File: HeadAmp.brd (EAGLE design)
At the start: 37.8 x 25.7 mm, 31 parts, among them U1 MAX97220A

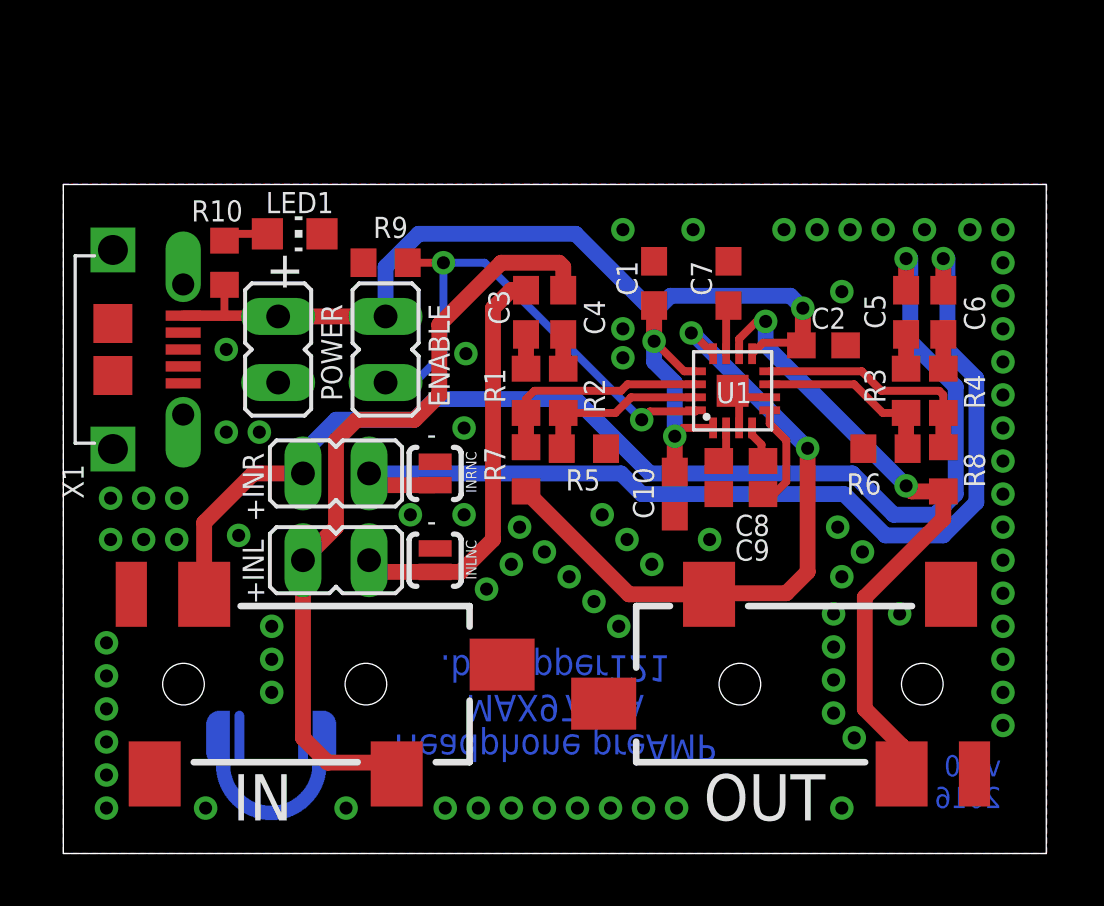
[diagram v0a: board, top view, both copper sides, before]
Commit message: Changed Gain to Max
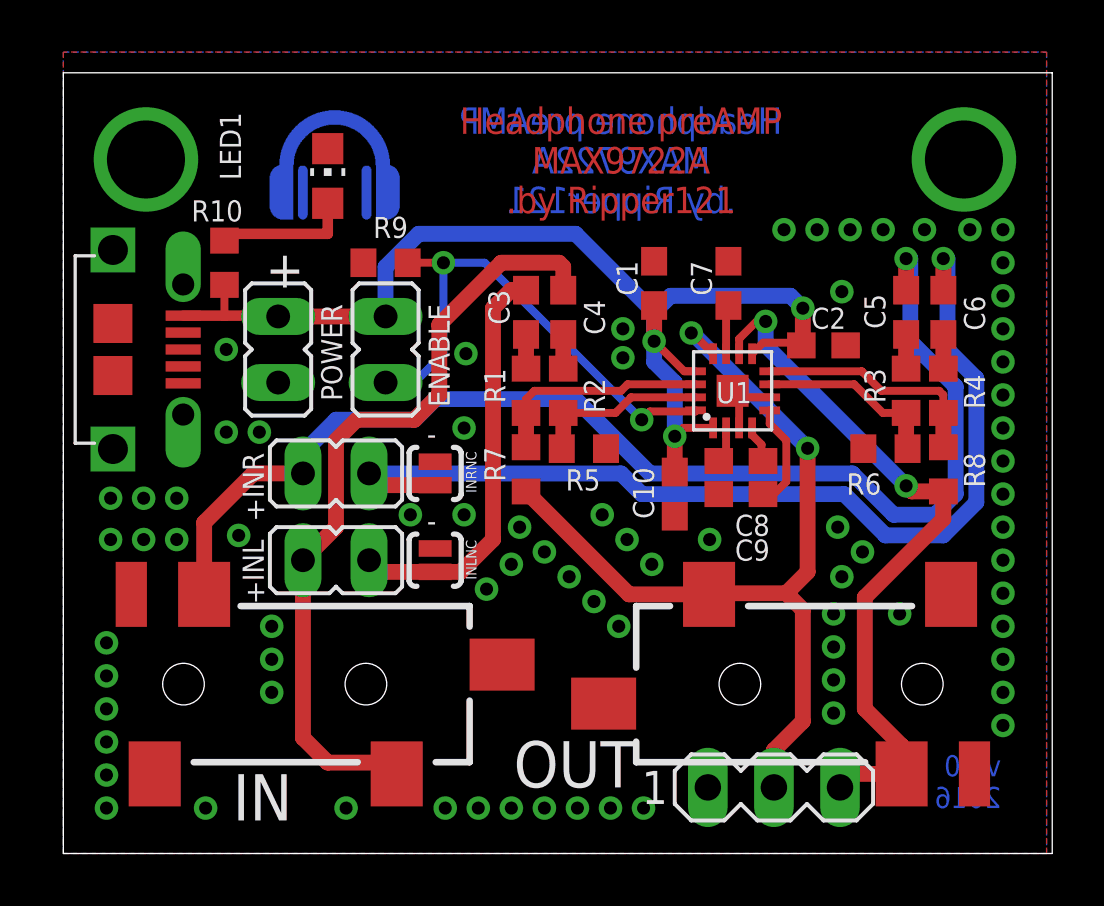
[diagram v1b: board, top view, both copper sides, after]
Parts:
- added SV1: (no value), con-lstb:MA03-1
- R1, R2, R3, R4: value 10k -> 4.7k
- R5, R6, R7, R8: value 10k -> 100k
- moved LED1 2.56 mm to (10.2, 26.0), turned to 0 degrees
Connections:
- removed net N$5: OUTRL.1, R8.2, U1.10
- removed net N$6: OUTRL.4, R7.2, U1.12
- new net LOUT: OUTRL.4, R7.2, SV1.2, U1.12
- new net ROUT: OUTRL.1, R8.2, SV1.3, U1.10
- net GND: now also SV1.1
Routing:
- net LOUT: track 0.00 -> 33.2 mm, vias 0 -> 2
- net ROUT: track 0.00 -> 27.4 mm, vias 0 -> 2
- net N$6: track 25.0 -> 0.00 mm, vias 2 -> 0
- net N$5: track 24.8 -> 0.00 mm, vias 2 -> 0
- net N$8: track 1.72 -> 5.22 mm
- net GND: vias 81 -> 78
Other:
- board size 37.8 x 25.7 mm -> 38 x 30 mm
